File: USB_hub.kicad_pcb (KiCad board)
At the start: 2 copper layers, 127.5 x 50.8 mm, 249 parts, among them J1 USB_SPI_(Opt), J10 USB3_A, J11 Conn_01x02_Socket, J12 USB_C_Receptacle, J13 I2C_HD3SS3220, J2 USB_C_Receptacle, J3 I2C_HD3SS3220, J4 USB_C_Receptacle, J5 I2C2_PD_Controller, J6 I2C_Mux, J7 I2C_EEPROM, J8 SD_Card_Receptacle, J9 USB3_A, Q1 SiRA24DP, Q2 SiRA12DP, SW1 RESET_HUB, SW2 FW_Upgrade, U1 USB7206C/KDX, U10 M24256-BWMN6P, U11 TPD4E02B04DQA, U12 TPD4E02B04DQA, U13 TPD4E02B04DQA, U14 TUSB1142IRNQR_C5216209, U15 GL3224-OIY04, U16 UCS2113-1-V/G4, U17 TPD4E02B04DQA, U18 TPD4E02B04DQA, U19 MCP19035-BAABE/MF, U2 MIC803-29D4VM3-TR, U20 TPS7A4701xRGW, U21 MIC23201YML-TR, U22 HD3SS3220IRNHR, U23 TPD4E02B04DQA, U24 TPD4E02B04DQA, U25 TPD4E02B04DQA, U3 HD3SS3220IRNHR, U4 TPS2068EDBVR, U5 TPD4E02B04DQA, U6 TPD4E02B04DQA, U7 TPD4E02B04DQA, U8 TVS2200DRV, U9 TPS25762CQRQLRQ1, Y1 25MHz, Y2 25MHz +-0.03%

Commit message: footprints grouped by the function
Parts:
- R1, R10, R11, R12, R13, R14, R15, R16, R17, R18, R19, R2, R20, R21, R22, R24, R25, R26, R27, R28, R29, R3, R30, R31, R32, R33, R34, R35, R36, R37, R38, R39, R4, R40, R41, R42, R43, R44, R45, R46, R47, R48, R49, R5, R50, R51, R52, R53, R54, R55, R56, R57, R58, R59, R6, R60, R61, R62, R63, R64, R65, R66, R67, R7, R8, R9: footprint Resistor_SMD:R_0603_1608Metric -> Resistor_SMD:R_0402_1005Metric
- R23: footprint Resistor_SMD:R_0603_1608Metric -> Resistor_SMD:R_1206_3216Metric
- moved C80 194.3 mm to (260.9, 130.6), turned to 90 degrees
- moved C79 183.4 mm to (249.3, 130.6), turned to 90 degrees
- moved C78 173.5 mm to (237.8, 130.6), turned to 90 degrees
- moved C77 164.6 mm to (226.2, 130.6), turned to 90 degrees
- moved C22 130.3 mm to (112.8, 168.1)
- moved U16 124.1 mm to (216.8, 130.9)
- moved NT1 122.2 mm to (-69.3, 22.8)
- moved C50 122.2 mm to (-99.3, 47.9)
- moved TP3 122.2 mm to (-57.5, 56.5)
- moved TP4 122.2 mm to (-57.5, 61.2)
- moved U9 122.2 mm to (-51.5, 36.3), turned to 180 degrees
- moved R2 122.0 mm to (235.3, 165.3), turned to -90 degrees
- moved R47 121.4 mm to (216.7, 135.4), turned to 90 degrees
- moved C81 121.1 mm to (219.9, 129.4), turned to 90 degrees
- moved J1 120.7 mm to (241.3, 162.3), turned to 180 degrees
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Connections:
- C20 pad 2: /USB7206C/XIN -> /USB7206C/XTALI
- C21 pad 2: /USB7206C/XOUT -> /USB7206C/XTALO
- Y1 pad 1: /USB7206C/XIN -> /USB7206C/XTALI
- Y1 pad 4: /USB7206C/XOUT -> /USB7206C/XTALO
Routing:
- net Net-(U1B-TEST1): track 0.00 -> 8.92 mm
- net Net-(U1B-TEST2): track 0.00 -> 7.05 mm
- net Net-(U1B-TEST3): track 0.00 -> 5.30 mm
- net GND: track 2.30 -> 4.57 mm

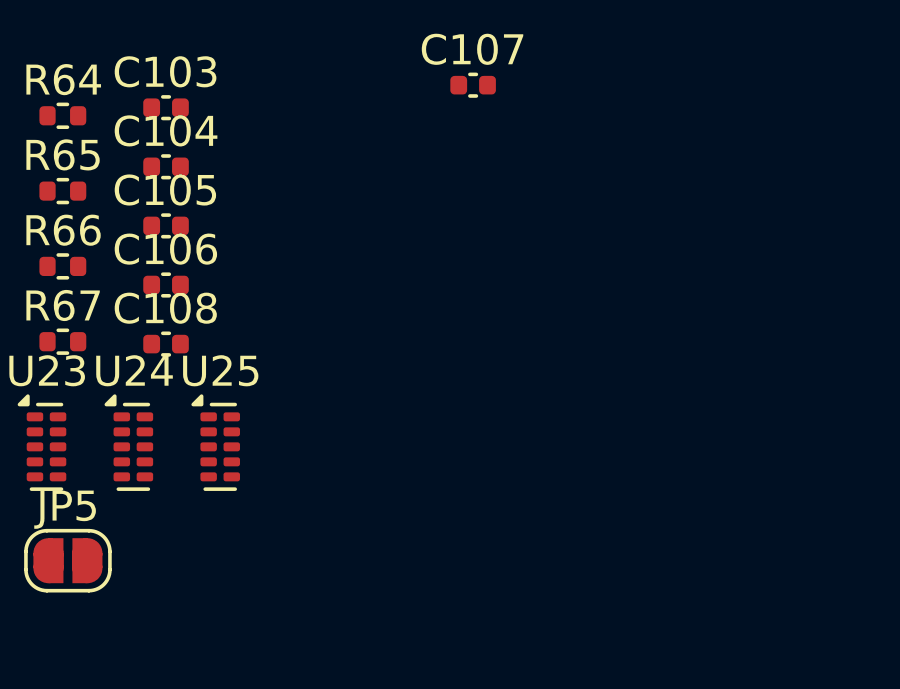
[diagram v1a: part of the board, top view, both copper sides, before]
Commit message: Scheme fixes
Fixed wrong connection of SNS pin of U21
USB7206c symbol improved
R7's value fixed
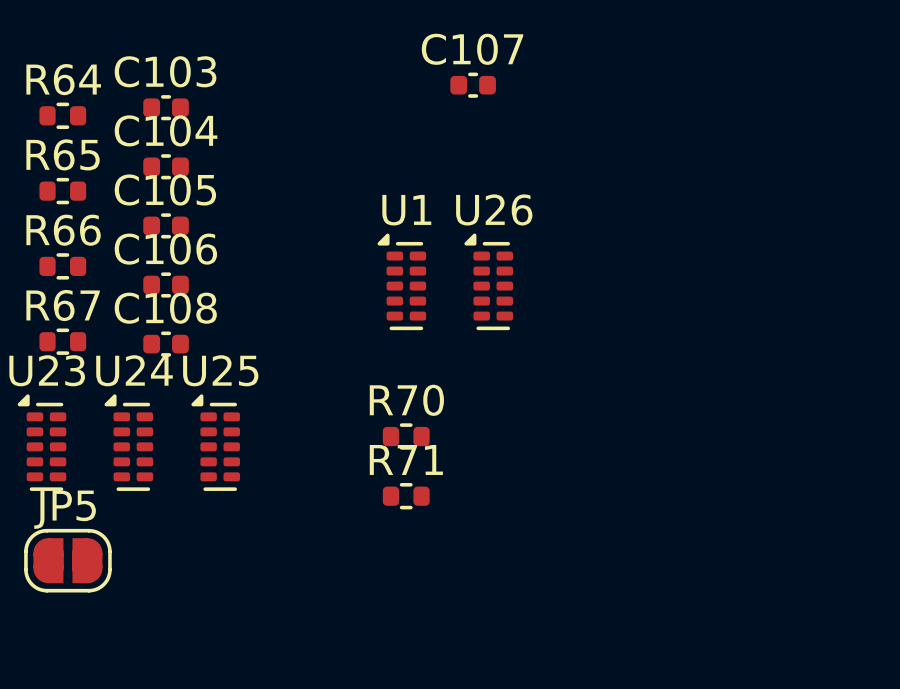
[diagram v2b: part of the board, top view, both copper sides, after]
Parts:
- added R70: 200k, Resistor_SMD:R_0402_1005Metric, F.Cu at (55.9, 132.4)
- added R71: 10k, Resistor_SMD:R_0402_1005Metric, F.Cu at (55.9, 134.4)
- added U1: TPD4E02B04DQA, Package_SON:USON-10_2.5x1.0mm_P0.5mm, F.Cu at (55.9, 127.4)
- added U26: TPD4E02B04DQA, Package_SON:USON-10_2.5x1.0mm_P0.5mm, F.Cu at (58.8, 127.4)
- R6: value 100k -> 200k
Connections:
- net Net-(U4-~{FLT}) renamed /USB-C1/~{FLT}
- J12 pad A6: /USB7206C/USB3UP.D+ -> /USB7206C/USB3_UP.D+
- J12 pad A7: /USB7206C/USB3UP.D- -> /USB7206C/USB3_UP.D-
- J12 pad B6: /USB7206C/USB3UP.D+ -> /USB7206C/USB3_UP.D+
- J12 pad B7: /USB7206C/USB3UP.D- -> /USB7206C/USB3_UP.D-
- R1 pad 1: Net-(U1B-RBIAS) -> Net-(U27-RBIAS)
- R1 pad 2: VSS -> GND
- R11 pad 1: VBUS_C1 -> +5V
- R2 pad 2: Net-(U1B-TEST1) -> Net-(U27-TEST1)
- R3 pad 2: Net-(U1B-TEST2) -> Net-(U27-TEST2)
- R4 pad 2: Net-(U1B-TEST3) -> Net-(U27-TEST3)
- U11 pad 10: unconnected-(U11-NC-Pad10) -> /USB-C2/USB-C2.RX1-
- U11 pad 6: unconnected-(U11-NC-Pad6) -> /USB-C2/USB-C2.TX1+
- U11 pad 7: unconnected-(U11-NC-Pad7) -> /USB-C2/USB-C2.TX1-
- U11 pad 9: unconnected-(U11-NC-Pad9) -> /USB-C2/USB-C2.RX1+
- U12 pad 10: unconnected-(U12-NC-Pad10) -> /USB-C2/USB-C2.RX2-
- U12 pad 6: unconnected-(U12-NC-Pad6) -> /USB-C2/USB-C2.TX2+
- U12 pad 7: unconnected-(U12-NC-Pad7) -> /USB-C2/USB-C2.TX2-
- U12 pad 9: unconnected-(U12-NC-Pad9) -> /USB-C2/USB-C2.RX2+
- U13 pad 10: unconnected-(U13-NC-Pad10) -> /USB-C2/USB-C2.CC1
- U13 pad 6: unconnected-(U13-NC-Pad6) -> /USB-C2/USB3_IN.D+
- U13 pad 7: unconnected-(U13-NC-Pad7) -> /USB-C2/USB3_IN.D-
- U13 pad 9: unconnected-(U13-NC-Pad9) -> /USB-C2/USB-C2.CC2
- U17 pad 10: unconnected-(U17-NC-Pad10) -> /USB-A1/USB-A1.RX1-
- U17 pad 6: unconnected-(U17-NC-Pad6) -> /USB-A1/USB-A1.TX1+
- U17 pad 7: unconnected-(U17-NC-Pad7) -> /USB-A1/USB-A1.TX1-
- U17 pad 9: unconnected-(U17-NC-Pad9) -> /USB-A1/USB-A1.RX1+
- U18 pad 10: unconnected-(U18-NC-Pad10) -> /USB-A1/USB-A2.RX1-
- U18 pad 6: unconnected-(U18-NC-Pad6) -> /USB-A1/USB-A2.TX1+
- U18 pad 7: unconnected-(U18-NC-Pad7) -> /USB-A1/USB-A2.TX1-
- U18 pad 9: unconnected-(U18-NC-Pad9) -> /USB-A1/USB-A2.RX1+
- U22 pad 10: /USB7206C/USB3UP.RX1- -> /USB7206C/USB3_UP.RX1-
- U22 pad 6: /USB7206C/USB3UP.TX1+ -> /USB7206C/USB3_UP.TX1+
- U22 pad 7: /USB7206C/USB3UP.TX1- -> /USB7206C/USB3_UP.TX1-
- U22 pad 9: /USB7206C/USB3UP.RX1+ -> /USB7206C/USB3_UP.RX1+
- U23 pad 10: unconnected-(U23-NC-Pad10) -> /USB-C_UP/USB-C_UP1/USB-C1.CC1
- U23 pad 6: unconnected-(U23-NC-Pad6) -> /USB-C_UP/USB-C_UP1/USB-C1.D+
- U23 pad 7: unconnected-(U23-NC-Pad7) -> /USB-C_UP/USB-C_UP1/USB-C1.D-
- U23 pad 9: unconnected-(U23-NC-Pad9) -> /USB-C_UP/USB-C_UP1/USB-C1.CC2
- U24 pad 10: unconnected-(U24-NC-Pad10) -> /USB-C_UP/USB-C_UP1/USB-C1.RX2-
- U24 pad 6: unconnected-(U24-NC-Pad6) -> /USB-C_UP/USB-C_UP1/USB-C1.TX2+
- U24 pad 7: unconnected-(U24-NC-Pad7) -> /USB-C_UP/USB-C_UP1/USB-C1.TX2-
- U24 pad 9: unconnected-(U24-NC-Pad9) -> /USB-C_UP/USB-C_UP1/USB-C1.RX2+
- U25 pad 10: unconnected-(U25-NC-Pad10) -> /USB-C_UP/USB-C_UP1/USB-C1.RX1-
- U25 pad 6: unconnected-(U25-NC-Pad6) -> /USB-C_UP/USB-C_UP1/USB-C1.TX1+
- U25 pad 7: unconnected-(U25-NC-Pad7) -> /USB-C_UP/USB-C_UP1/USB-C1.TX1-
- U25 pad 9: unconnected-(U25-NC-Pad9) -> /USB-C_UP/USB-C_UP1/USB-C1.RX1+
- U5 pad 10: unconnected-(U5-NC-Pad10) -> /USB-C1/USB-C1.CC1
- U5 pad 6: unconnected-(U5-NC-Pad6) -> /USB-C1/USB-C1.D+
- U5 pad 7: unconnected-(U5-NC-Pad7) -> /USB-C1/USB-C1.D-
- U5 pad 9: unconnected-(U5-NC-Pad9) -> /USB-C1/USB-C1.CC2
- U6 pad 10: unconnected-(U6-NC-Pad10) -> /USB-C1/USB-C1.RX2-
- U6 pad 6: unconnected-(U6-NC-Pad6) -> /USB-C1/USB-C1.TX2+
- U6 pad 7: unconnected-(U6-NC-Pad7) -> /USB-C1/USB-C1.TX2-
- U6 pad 9: unconnected-(U6-NC-Pad9) -> /USB-C1/USB-C1.RX2+
- U7 pad 10: unconnected-(U7-NC-Pad10) -> /USB-C1/USB-C1.RX1-
- U7 pad 6: unconnected-(U7-NC-Pad6) -> /USB-C1/USB-C1.TX1+
- U7 pad 7: unconnected-(U7-NC-Pad7) -> /USB-C1/USB-C1.TX1-
- U7 pad 9: unconnected-(U7-NC-Pad9) -> /USB-C1/USB-C1.RX1+

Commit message: Board set-up setted, Scheme pdf exported,
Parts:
- removed the C101 at (58.6, 109.9)
- removed the C102 at (22.9, 114.7)
- removed the C103 at (47.9, 121.5)
- removed the C82 at (181.7, 13.5)
- removed the C83 at (181.7, 12.4)
- removed the C84 at (176.6, 12.3)
- removed JP3: SMCLK, Jumper:SolderJumper-2_P1.3mm_Open_Pad1.0x1.5mm
- removed JP4: SM_BUS or Standalone, Jumper:SolderJumper-3_P1.3mm_Open_RoundedPad1.0x1.5mm_NumberLabels
- removed JP5: Connect to I2C mode, Jumper:SolderJumper-2_P1.3mm_Open_RoundedPad1.0x1.5mm
- removed Q2: SiRA12DP, Package_SO:PowerPAK_SO-8_Single
- removed the R47 at (216.7, 135.4)
- removed the R50 at (212.1, 123.4)
- removed the R51 at (212.2, 120.8)
- removed the R52 at (184.5, 9.50)
- removed the R53 at (180.1, 12.9)
- removed the R54 at (173.8, 14.1)
- removed the R55 at (173.8, 12.3)
- removed the R56 at (178.6, 11.5)
- removed the R57 at (186.2, 17.0)
- removed the R62 at (55.2, 110.2)
- removed the R63 at (55.2, 112.7)
- removed TP13: Out2, TestPoint:TestPoint_2Pads_Pitch5.08mm_Drill1.3mm
- removed the TP7 at (215.4, 11.0)
- removed the U1 at (55.9, 127.4)
- removed the U1 at (219.2, 165.2)
- removed the U19 at (186.8, 12.8)
- removed the U20 at (171.1, 45.0)
- removed the U25 at (49.7, 132.8)
- added C100: 1uF, Capacitor_SMD:C_0402_1005Metric, F.Cu at (352.6, -21.5)
- added C109: 47uF, Capacitor_SMD:C_0402_1005Metric, F.Cu at (355.4, -23.4)
- added C110: 47uF, Capacitor_SMD:C_0402_1005Metric, F.Cu at (355.4, -21.5)
- added C111: 47uF, Capacitor_SMD:C_0402_1005Metric, F.Cu at (355.4, -19.5)
- added C112: 100nF, Capacitor_SMD:C_0402_1005Metric, F.Cu at (374.6, -24.5)
- added C113: 22nF, Capacitor_SMD:C_0402_1005Metric, F.Cu at (376.3, -25.1)
- added C121: 100uF, Capacitor_THT:C_Radial_D10.0mm_H16.0mm_P5.00mm, F.Cu at (443.8, 38.8)
- added C122: 100nF, Capacitor_SMD:C_0402_1005Metric, F.Cu at (450.9, 21.4)
- added C123: 100nF, Capacitor_SMD:C_0402_1005Metric, F.Cu at (450.9, 23.3)
- added C124: 100nF, Capacitor_SMD:C_0402_1005Metric, F.Cu at (450.9, 25.3)
- added C125: 100nF, Capacitor_SMD:C_0402_1005Metric, F.Cu at (450.9, 27.3)
- added C126: 100nF, Capacitor_SMD:C_0402_1005Metric, F.Cu at (450.9, 29.2)
- added C20: 10uF, Capacitor_SMD:C_0402_1005Metric, F.Cu at (443.7, 55.8)
- added C74: 330nF, Capacitor_SMD:C_0402_1005Metric, F.Cu at (403.3, 61.8)
- added C75: 330nF, Capacitor_SMD:C_0402_1005Metric, F.Cu at (403.3, 63.8)
- added C91: 1u, Capacitor_SMD:C_0402_1005Metric, F.Cu at (478.0, -40.7)
- added C92: 0.1u, Capacitor_SMD:C_0402_1005Metric, F.Cu at (479.3, -40.7)
- added C93: 1u, Capacitor_SMD:C_0402_1005Metric, F.Cu at (478.0, -48.5)
- added C94: 0.1u, Capacitor_SMD:C_0402_1005Metric, F.Cu at (479.3, -48.5)
- added C95: 1uF, Capacitor_SMD:C_0402_1005Metric, F.Cu at (378.6, -22.6)
- added C96: 10uF, Capacitor_SMD:C_0402_1005Metric, F.Cu at (349.7, -15.6)
- added C97: 10uF, Capacitor_SMD:C_0402_1005Metric, F.Cu at (349.7, -13.6)
- added C98: 10uF, Capacitor_SMD:C_0402_1005Metric, F.Cu at (349.7, -11.6)
- added C99: 1uF, Capacitor_SMD:C_0402_1005Metric, F.Cu at (352.6, -23.4)
- added D1: ESD441DPLR, EasyEDA:X2SON-2_L0.6-W0.3-P0.35, F.Cu at (443.2, 57.6)
- added D12: B520C-13-F, Diode_SMD:D_SMC, F.Cu at (573.9, 58.8)
- added D13: SMCJ12A, Diode_SMD:D_SMC, F.Cu at (539.2, 61.3)
- added D14: GREEN, LED_SMD:LED_0603_1608Metric, F.Cu at (486.9, 142.6)
- added D15: GREEN, LED_SMD:LED_0603_1608Metric, F.Cu at (553.2, 85.3)
- added D16: GREEN, LED_SMD:LED_0603_1608Metric, F.Cu at (553.2, 87.4)
- added D17: GREEN, LED_SMD:LED_0603_1608Metric, F.Cu at (553.2, 89.3)
- added D2: ESD441DPLR, EasyEDA:X2SON-2_L0.6-W0.3-P0.35, F.Cu at (396.8, 62.5)
- added D3: LED, LED_SMD:LED_0603_1608Metric, F.Cu at (397.9, 57.8)
- added D4: GREEN, LED_SMD:LED_0603_1608Metric, F.Cu at (397.9, 60.4)
- added FB1: 7427934, SamacSys_Parts:7427934, F.Cu at (470.7, -55.5)
- added FB2: 7427934, SamacSys_Parts:7427934, F.Cu at (470.8, -38.5)
- added FB3: 7427934, SamacSys_Parts:7427934, F.Cu at (470.8, -46.4)
- added R13: 200k, Resistor_SMD:R_0402_1005Metric, F.Cu at (394.4, 57.5)
- added R17: 5k, Resistor_SMD:R_0402_1005Metric, F.Cu at (394.4, 59.5)
- added R18: 4.7k, Resistor_SMD:R_0402_1005Metric, F.Cu at (394.4, 61.5)
- added R19: 1.5k, Resistor_SMD:R_0402_1005Metric, F.Cu at (394.4, 63.5)
- added R20: 4.7k, Resistor_SMD:R_0402_1005Metric, F.Cu at (394.4, 65.5)
- added R35: 4.7k, Resistor_SMD:R_0402_1005Metric, F.Cu at (448.6, 51.8)
- added R36: 4.7k, Resistor_SMD:R_0402_1005Metric, F.Cu at (448.6, 53.8)
- added R37: 4.7k, Resistor_SMD:R_0402_1005Metric, F.Cu at (448.6, 55.8)
- added R38: 4.7k, Resistor_SMD:R_0402_1005Metric, F.Cu at (448.6, 57.8)
- added R43: 1k, Resistor_SMD:R_0402_1005Metric, F.Cu at (448.6, 59.8)
- added R5: 33k, Resistor_SMD:R_0402_1005Metric, F.Cu at (443.7, 51.8)
- added R59: 520, Resistor_SMD:R_0402_1005Metric, F.Cu at (406.2, 61.8)
- added R6: 50k, Resistor_SMD:R_0402_1005Metric, F.Cu at (443.7, 53.8)
- added R68: 2, Resistor_SMD:R_0402_1005Metric, F.Cu at (478.0, -59.3)
- added R69: 200, Resistor_SMD:R_0402_1005Metric, F.Cu at (558.4, 58.0)
- added R70: 27k, Resistor_SMD:R_0402_1005Metric, F.Cu at (548.1, 60.3)
- added R71: 47k, Resistor_SMD:R_0402_1005Metric, F.Cu at (548.1, 61.5)
- added R72: 100 1%, Resistor_SMD:R_0402_1005Metric, F.Cu at (552.3, 63.4)
- added R73: 549 1%, Resistor_SMD:R_0402_1005Metric, F.Cu at (553.5, 63.4)
- added R74: 2, Resistor_SMD:R_0402_1005Metric, F.Cu at (478.7, -42.3)
- added R75: 2, Resistor_SMD:R_0402_1005Metric, F.Cu at (478.7, -50.2)
- added R76: 290k, Resistor_SMD:R_0402_1005Metric, F.Cu at (378.0, -20.7)
- added R77: 10k, Resistor_SMD:R_0402_1005Metric, F.Cu at (370.8, -21.2)
- added R78: 5k, Resistor_SMD:R_0402_1005Metric, F.Cu at (372.2, -25.3)
- added R79: 680, Resistor_SMD:R_0402_1005Metric, F.Cu at (372.9, -23.5)
- added R80: 243k, Resistor_SMD:R_0402_1005Metric, F.Cu at (376.3, -24.0)
- added R81: R, Resistor_SMD:R_0402_1005Metric, F.Cu at (376.3, -22.9)
- added R82: 560, Resistor_SMD:R_0402_1005Metric, F.Cu at (486.7, 140.8)
- added R83: 10k, Resistor_SMD:R_0402_1005Metric, F.Cu at (487.6, 144.4)
- added R84: 4.7k, Resistor_SMD:R_0402_1005Metric, F.Cu at (550.3, 85.3)
- added R85: 1.5k, Resistor_SMD:R_0402_1005Metric, F.Cu at (550.3, 87.4)
- added R86: 560, Resistor_SMD:R_0402_1005Metric, F.Cu at (550.3, 89.3)
- added R87: 1M, Resistor_SMD:R_0402_1005Metric, F.Cu at (491.5, 146.2)
- added R92: 900k, Resistor_SMD:R_0402_1005Metric, F.Cu at (439.1, 34.0)
- added R93: 200k, Resistor_SMD:R_0402_1005Metric, F.Cu at (439.1, 36.0)
- added R94: 200k, Resistor_SMD:R_0402_1005Metric, F.Cu at (439.1, 38.0)
- added R95: 4.7k, Resistor_SMD:R_0402_1005Metric, F.Cu at (439.1, 40.0)
- added R96: 4.7k, Resistor_SMD:R_0402_1005Metric, F.Cu at (439.1, 42.0)
- added R97: 4.7k, Resistor_SMD:R_0402_1005Metric, F.Cu at (439.1, 44.0)
- added TP9: 0 when there is a connected device & port is fuctioning as 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, TestPoint:TestPoint_Loop_D1.80mm_Drill1.0mm_Beaded, F.Cu at (430.2, 22.7)
- added U1: USB7206C/KDX, SamacSys_Parts:QFN40P1200X1200X90-101N-D, F.Cu at (219.1, 165.3)
- added U16: TPD4E02B04DQA, Package_SON:USON-10_2.5x1.0mm_P0.5mm, F.Cu at (403.3, 58.8)
- added U17: TPD4E02B04DQA, Package_SON:USON-10_2.5x1.0mm_P0.5mm, F.Cu at (406.2, 58.8)
- added U21: SiRA80DP, Package_SO:PowerPAK_SO-8L_Single, F.Cu at (563.2, 53.1)
- added U27: TPD4E02B04DQA, Package_SON:USON-10_2.5x1.0mm_P0.5mm, F.Cu at (442.0, 46.8)
- added U28: TPD4E02B04DQA, Package_SON:USON-10_2.5x1.0mm_P0.5mm, F.Cu at (444.9, 46.8)
- added U29: TPD4E02B04DQA, Package_SON:USON-10_2.5x1.0mm_P0.5mm, F.Cu at (447.8, 46.8)
- C102: renamed from C91; value 47uF -> 4.7uF
- C104: value 100nF -> 820pF
- C105: value 100nF -> C
- C106, C107, C108: value 100nF -> 47uF
- C42: renamed from C41; value 0.1uF (10V) -> 0.1uF (50V)
- C44: renamed from C43; value 0.1uF (10V) -> 0.1uF (50V)
- C85: value 0.33uF -> 1u
- C86: value 100uF -> 0.1u; footprint Capacitor_THT:C_Radial_D10.0mm_H16.0mm_P5.00mm -> Capacitor_SMD:C_0402_1005Metric
- C87, C88: value 100uF -> 2.2nF; footprint Capacitor_THT:C_Radial_D10.0mm_H16.0mm_P5.00mm -> Capacitor_SMD:C_0402_1005Metric
- C89: value 0.1uF -> 8.20nF
- C90: value 4.7uF -> 4.3nF
- D5: renamed from D1; value LED -> GREEN
- D6: value SMBJP6KE6.8 -> GREEN; footprint Diode_SMD:D_SMB -> LED_SMD:LED_0603_1608Metric
- D7: value ESD441DPLR -> GREEN; footprint EasyEDA:X2SON-2_L0.6-W0.3-P0.35 -> LED_SMD:LED_0603_1608Metric
- J1: footprint Connector_PinHeader_1.27mm:PinHeader_1x05_P1.27mm_Vertical -> Connector_PinHeader_1.27mm:PinHeader_1x06_P1.27mm_Vertical
- J10, J9: footprint Connector_USB:USB3_A_Molex_48393-001 -> SamacSys_Parts:GSB4116344HR
- J11: value Conn_01x02_Socket -> 8-pin ATX connector; footprint Connector_PinHeader_1.27mm:PinHeader_1x02_P1.27mm_Vertical -> SamacSys_Parts:45586-000Y
- J2, J4: footprint Connector_USB:USB_C_Receptacle_Amphenol_12401610E4-2A -> SamacSys_Parts:USB420003A
- JP2: value SMDATA -> Connect to I2C mode; footprint Jumper:SolderJumper-2_P1.3mm_Open_Pad1.0x1.5mm -> Jumper:SolderJumper-2_P1.3mm_Open_RoundedPad1.0x1.5mm
- L2: value 2uH -> 4.7nH
- Q1: value SiRA24DP -> MMBT2222A; footprint Package_SO:PowerPAK_SO-8_Single -> Package_TO_SOT_SMD:SOT-23-3
- R11: renamed from R7; value 900 -> 900k
- R34: renamed from R25; value R -> 1k
- R64: value 900k -> 1.5k
- R65: value 200k -> 1.5k
- R66: value 200k -> 10k
- R67: value 4.7k -> 499k
- TP1, TP2: footprint TestPoint:TestPoint_2Pads_Pitch5.08mm_Drill1.3mm -> TestPoint:TestPoint_Loop_D1.80mm_Drill1.0mm_Beaded
- TP10: value 0 when there is a connected device & port is fuctioning as DFP -> 0 when overvurrent on VCONN detected; footprint TestPoint:TestPoint_2Pads_Pitch5.08mm_Drill1.3mm -> TestPoint:TestPoint_Loop_D1.80mm_Drill1.0mm_Beaded
- TP11: value 0 when overvurrent on VCONN detected -> Out1; footprint TestPoint:TestPoint_2Pads_Pitch5.08mm_Drill1.3mm -> TestPoint:TestPoint_Loop_D1.80mm_Drill1.0mm_Beaded
- TP12: value Out1 -> Out2; footprint TestPoint:TestPoint_2Pads_Pitch5.08mm_Drill1.3mm -> TestPoint:TestPoint_Loop_D1.80mm_Drill1.0mm_Beaded
- TP3, TP4, TP5, TP6: footprint TestPoint:TestPoint_THTPad_1.5x1.5mm_Drill0.7mm -> TestPoint:TestPoint_Loop_D1.80mm_Drill1.0mm_Beaded
- TP7: renamed from TP8; footprint TestPoint:TestPoint_THTPad_1.5x1.5mm_Drill0.7mm -> TestPoint:TestPoint_Loop_D1.80mm_Drill1.0mm_Beaded
- TP8: renamed from TP9; footprint TestPoint:TestPoint_THTPad_1.5x1.5mm_Drill0.7mm -> TestPoint:TestPoint_Loop_D1.80mm_Drill1.0mm_Beaded
- U10: value M24256-BWMN6P -> 24LC256
- U18: renamed from U16; value UCS2113-1-V/G4 -> UCS2114-1-V/G4
- U22: value HD3SS3220IRNHR -> TPS25983; footprint footprints:RNH0030A -> SamacSys_Parts:TPS259830ONRGER
- U23: value TPD4E02B04DQA -> AP7361C-33E; footprint Package_SON:USON-10_2.5x1.0mm_P0.5mm -> Package_TO_SOT_SMD:SOT-223-3_TabPin2
- U24: value TPD4E02B04DQA -> MP8795; footprint Package_SON:USON-10_2.5x1.0mm_P0.5mm -> Package_DFN_QFN:MPS-QFN-21_3x4mm
- U26: value TPD4E02B04DQA -> HD3SS3220IRNHR; footprint Package_SON:USON-10_2.5x1.0mm_P0.5mm -> footprints:RNH0030A
- moved U22 526.1 mm to (553.2, 58.5)
- moved R66 518.2 mm to (558.4, 60.3), turned to 180 degrees
- moved R67 508.5 mm to (548.1, 59.1)
- moved R65 506.8 mm to (550.2, 91.4)
- moved R64 506.5 mm to (550.2, 93.3)
- moved D7 495.5 mm to (553.2, 91.4), turned to 180 degrees
- moved J12 419.1 mm to (443.6, 26.8)
- moved TP10 418.0 mm to (430.2, 27.3)
- moved TP11 418.0 mm to (430.2, 32.0)
- moved TP12 418.0 mm to (430.2, 36.6)
- moved J13 408.3 mm to (434.4, 40.6)
- moved U26 380.9 mm to (430.1, 42.2)
- moved C90 366.6 mm to (551.2, 63.4), turned to -90 degrees
- moved U24 361.6 mm to (374.7, -19.8), turned to -90 degrees
- moved C104 357.9 mm to (373.5, -25.3), turned to 90 degrees
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- renumbered C93 to C101, C92 to C103, C94 to C114, C95 to C115, C96 to C116, C97 to C117, C98 to C118, C99 to C119, C100 to C120, C20 to C21, C21 to C22, C22 to C23, C23 to C24, C24 to C25, C25 to C26, C26 to C27, C27 to C28, C28 to C29, C29 to C30, C30 to C31, C31 to C32, C32 to C33, C33 to C34, C34 to C35, C35 to C36, C36 to C37, C37 to C38, C38 to C39, C39 to C40, C40 to C41, C42 to C43, C44 to C45, C45 to C46, C46 to C47, C47 to C48, C48 to C49, C49 to C50, C50 to C51, C51 to C52, C52 to C53, C53 to C54, C54 to C55, C55 to C56, C56 to C57, C57 to C58, C58 to C59, C59 to C60, C60 to C61, C61 to C62, C62 to C63, C63 to C64, C64 to C65, C65 to C66, C66 to C67, C67 to C68, C68 to C69, C69 to C70, C70 to C71, C71 to C72, C72 to C73, C73 to C76, C74 to C77, C75 to C78, C76 to C79, C77 to C80, C78 to C81, C79 to C82, C80 to C83, C81 to C84, D4 to D10, D5 to D11, D2 to D8, D3 to D9, R6 to R10, R8 to R12, R9 to R14, R10 to R15, R11 to R16, R12 to R21, R13 to R22, R14 to R23, R15 to R24, R16 to R25, R17 to R26, R18 to R27, R19 to R28, R20 to R29, R21 to R30, R22 to R31, R23 to R32, R24 to R33, R26 to R39, R27 to R40, R28 to R41, R29 to R42, R30 to R44, R31 to R45, R32 to R46, R33 to R47, R34 to R48, R35 to R49, R36 to R50, R37 to R51, R38 to R52, R39 to R53, R40 to R54, R41 to R55, R42 to R56, R43 to R57, R44 to R58, R45 to R60, R46 to R61, R48 to R62, R49 to R63, R71 to R7, R5 to R8, R58 to R88, R59 to R89, R70 to R9, R60 to R90, R61 to R91, U17 to U19, U18 to U20, U21 to U25
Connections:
- net /USB7206C/USB3_UP.D+ renamed /USB-C_UP1/USB3_IN.D+
- net /USB7206C/USB3_UP.D- renamed /USB-C_UP1/USB3_IN.D-
- C101 pad 1: Net-(U20-NR) -> +5V_Power
- C104 pad 1: Net-(U22-TX1P) -> Net-(U24-FB)
- C104 pad 2: /USB-C_UP/USB-C_UP1/USB-C1.TX1+ -> +5V_prefiltered
- C105 pad 1: Net-(U22-TX1N) -> Net-(U24-VCC)
- C105 pad 2: /USB-C_UP/USB-C_UP1/USB-C1.TX1- -> GND
- C106 pad 1: Net-(U22-TX2P) -> +5V_prefiltered
- C106 pad 2: /USB-C_UP/USB-C_UP1/USB-C1.TX2+ -> GND
- C107 pad 1: Net-(U22-TX2N) -> +5V_prefiltered
- C107 pad 2: /USB-C_UP/USB-C_UP1/USB-C1.TX2- -> GND
- C108 pad 1: Net-(U22-TX2N) -> +5V_prefiltered
- C108 pad 2: /USB-C_UP/USB-C_UP1/USB-C1.TX2- -> GND
- C114 pad 1: +5V -> +5V_Power
- C115 pad 1: +5V -> +5V_Power
- C116 pad 1: +5V -> +5V_Power
- C119 pad 1: +5V -> +5V_Power
- C23 pad 1: +5V -> +5V_USB_C_SD
- C24 pad 1: +5V -> +5V_USB_C_SD
- C29 pad 1: +5V -> +5V_USB_C_SD
- C30 pad 1: +5V -> +5V_USB_C_SD
- C80 pad 1: +5V -> +5V_USB_A
- C81 pad 1: +5V -> +5V_USB_A
- C82 pad 1: +5V -> +5V_USB_A
- C83 pad 1: +5V -> +5V_USB_A
- C84 pad 1: +5V -> +5V_USB_A
- C85 pad 1: Net-(U19-BOOT) -> +5V_USB_A
- C85 pad 2: /Power/PHASE -> Net-(C85-Pad2)
- C86 pad 1: +5V -> +5V_USB_A
- C87 pad 1: +5V -> Net-(U22-NRETRY)
- C88 pad 1: +5V -> Net-(U22-RETRY_DLY)
- C89 pad 1: +5V -> Net-(U22-dVdt)
- C90 pad 1: GND -> Net-(U22-ITIMER)
- C90 pad 2: Net-(U19-+VCC) -> GND
- D5 pad 2: /SD-interface/LED -> Net-(D5-A)
- D6 pad 2: +5V -> Net-(D6-A)
- D7 pad 1: VBUS_UP -> GND
- D7 pad 2: GND -> Net-(D7-A)
- J11 pad 1: GND -> Net-(D13-C)
- J11 pad 2: +12V -> Net-(D13-C)
- J12 pad A10: /USB-C_UP/USB-C_UP1/USB-C1.RX2- -> /USB-C_UP1/USB-C1.RX2-
- J12 pad A11: /USB-C_UP/USB-C_UP1/USB-C1.RX2+ -> /USB-C_UP1/USB-C1.RX2+
- J12 pad A2: /USB-C_UP/USB-C_UP1/USB-C1.TX1+ -> /USB-C_UP1/USB-C1.TX1+
- J12 pad A3: /USB-C_UP/USB-C_UP1/USB-C1.TX1- -> /USB-C_UP1/USB-C1.TX1-
- J12 pad A5: /USB-C_UP/USB-C_UP1/USB-C1.CC1 -> /USB-C_UP1/USB-C1.CC1
- J12 pad B10: /USB-C_UP/USB-C_UP1/USB-C1.RX1- -> /USB-C_UP1/USB-C1.RX1-
- J12 pad B11: /USB-C_UP/USB-C_UP1/USB-C1.RX1+ -> /USB-C_UP1/USB-C1.RX1+
- J12 pad B2: /USB-C_UP/USB-C_UP1/USB-C1.TX2+ -> /USB-C_UP1/USB-C1.TX2+
- J12 pad B3: /USB-C_UP/USB-C_UP1/USB-C1.TX2- -> /USB-C_UP1/USB-C1.TX2-
- J12 pad B5: /USB-C_UP/USB-C_UP1/USB-C1.CC2 -> /USB-C_UP1/USB-C1.CC2
- J13 pad 1: /USB-C_UP/USB-C_UP1/I2C_HD3SS3220.SDA -> /USB-C_UP1/I2C_HD3SS3220.SDA
- J13 pad 2: /USB-C_UP/USB-C_UP1/I2C_HD3SS3220.SCL -> /USB-C_UP1/I2C_HD3SS3220.SCL
- J13 pad 3: /USB-C_UP/USB-C_UP1/I2C_HD3SS3220.INT_N -> /USB-C_UP1/I2C_HD3SS3220.INT_N
- JP2 pad 1: Net-(JP2-A) -> +5V_USB_C_SD
- JP2 pad 2: /USB-A1/SMBUS.SDA -> /USB-C_UP1/ADDR
- L2 pad 1: /Power/PHASE -> Net-(U24-SW)
- L2 pad 2: +5V -> +5V_prefiltered
- L3 pad 1: Net-(U21-SNS) -> Net-(U25-SW)
- Q1 pad 1: /Power/PHASE -> Net-(D14-K)
- Q1 pad 2: /Power/PHASE -> Net-(Q1-B)
- Q1 pad 3: /Power/PHASE -> GND
- R14 pad 1: +5V -> +5V_USB_C_SD
- R15 pad 1: +5V -> +5V_USB_C_SD
- R16 pad 1: +5V -> +5V_USB_C_SD
- R60 pad 2: /USB-A1/PRT_CTR1 -> /USB-A1/PRT_EN1
- R63 pad 1: /USB-A1/PRT_CTR2 -> /USB-A1/PRT_EN2
- R64 pad 1: Net-(U22-VBUS_DET) -> VBUS-A1
- R64 pad 2: VBUS_C1 -> Net-(D6-A)
- R65 pad 1: Net-(U22-DIR) -> VBUS-A2
- R65 pad 2: +3V3 -> Net-(D7-A)
- R66 pad 1: /USB-C_UP/USB-C_UP1/I2C_HD3SS3220.INT_N -> +3V3
- R66 pad 2: +3V3 -> Net-(U22-PG)
- R67 pad 1: GND -> Net-(D13-C)
- R67 pad 2: Net-(U22-PORT) -> Net-(U22-EN/UVLO)
- R88 pad 1: +5V -> +5V_Power
- TP10 pad 1: /USB-C_UP/USB-C_UP1/ID -> /USB-C_UP1/VCONN_FAULT_N
- TP11 pad 1: /USB-C_UP/USB-C_UP1/VCONN_FAULT_N -> /USB-C_UP1/I2C_HD3SS3220.SDA
- TP12 pad 1: /USB-C_UP/USB-C_UP1/I2C_HD3SS3220.SDA -> /USB-C_UP1/I2C_HD3SS3220.SCL
- U14 pad 4: unconnected-(U14-~{SLP_S0}-Pad4) -> Net-(U14-~{SLP_S0})
- U15 pad 1: /SD-interface/USB-SD.TX1- -> Net-(U15-TXN)
- U15 pad 2: /SD-interface/USB-SD.TX1+ -> Net-(U15-TXP)
- U18 pad 10: +5V -> +5V_USB_A
- U18 pad 13: /USB-A1/COMM_ILIM -> +5V_USB_A
- U18 pad 17: Net-(JP3-A) -> GND
- U18 pad 18: Net-(JP2-A) -> GND
- U18 pad 3: Net-(U16-~{BOOST}) -> GND
- U18 pad 6: +5V -> +5V_USB_A
- U18 pad 7: +5V -> +5V_USB_A
- U18 pad 8: +5V -> +5V_USB_A
- U18 pad 9: +5V -> +5V_USB_A
- U22 pad 1: /USB-C_UP/USB-C_UP1/USB-C1.CC2 -> Net-(D13-C)
- U22 pad 10: /USB7206C/USB3_UP.RX1- -> Net-(U22-RETRY_DLY)
- U22 pad 11: Net-(U22-DIR) -> Net-(U22-NRETRY)
- U22 pad 12: GND -> Net-(U22-OVLO)
- U22 pad 13: GND -> Net-(U22-PG)
- U22 pad 14: /USB-C_UP/USB-C_UP1/USB-C1.RX1- -> GND
- U22 pad 15: /USB-C_UP/USB-C_UP1/USB-C1.RX1+ -> Net-(U22-dVdt)
- U22 pad 16: Net-(U22-TX1N) -> (no net)
- U22 pad 17: Net-(U22-TX1P) -> Net-(U21-S-Pad1)
- U22 pad 18: /USB-C_UP/USB-C_UP1/USB-C1.RX2- -> Net-(U21-S-Pad1)
- U22 pad 19: /USB-C_UP/USB-C_UP1/USB-C1.RX2+ -> Net-(U21-S-Pad1)
- U22 pad 2: /USB-C_UP/USB-C_UP1/USB-C1.CC1 -> Net-(D13-C)
- U22 pad 20: Net-(U22-TX2N) -> Net-(U21-S-Pad1)
- U22 pad 21: Net-(U22-TX2P) -> Net-(U21-S-Pad1)
- U22 pad 22: /USB-C_UP/USB-C_UP1/ADDR -> Net-(U21-S-Pad1)
- U22 pad 23: /USB-C_UP/USB-C_UP1/I2C_HD3SS3220.INT_N -> Net-(U21-S-Pad1)
- U22 pad 24: /USB-C_UP/USB-C_UP1/VCONN_FAULT_N -> Net-(U21-S-Pad1)
- U22 pad 25: /USB-C_UP/USB-C_UP1/I2C_HD3SS3220.SDA -> Net-(U21-S-Pad1)
- U22 pad 26: /USB-C_UP/USB-C_UP1/I2C_HD3SS3220.SCL -> GND
- U22 pad 3: unconnected-(U22-CURRENT_MODE-Pad3) -> Net-(D13-C)
- U22 pad 4: Net-(U22-PORT) -> GND
- U22 pad 5: Net-(U22-VBUS_DET) -> GND
- U22 pad 6: /USB7206C/USB3_UP.TX1+ -> Net-(U22-EN/UVLO)
- U22 pad 7: /USB7206C/USB3_UP.TX1- -> Net-(U22-ITIMER)
- U22 pad 8: +3V3 -> Net-(U22-ILIM)
- U22 pad 9: /USB7206C/USB3_UP.RX1+ -> Net-(U22-IMON)
- U23 pad 1: /USB-C_UP/USB-C_UP1/USB-C1.CC1 -> +5V_Power
- U23 pad 2: /USB-C_UP/USB-C_UP1/USB-C1.CC2 -> GND
- U23 pad 3: GND -> +3V3
- U24 pad 1: /USB-C_UP/USB-C_UP1/USB-C1.RX2- -> Net-(U24-BST)
- U24 pad 10: /USB-C_UP/USB-C_UP1/USB-C1.RX2- -> +12V
- U24 pad 2: /USB-C_UP/USB-C_UP1/USB-C1.RX2+ -> AGND
- U24 pad 3: GND -> Net-(U24-CS)
- U24 pad 4: /USB-C_UP/USB-C_UP1/USB-C1.TX2- -> Net-(U24-MODE)
- U24 pad 5: /USB-C_UP/USB-C_UP1/USB-C1.TX2+ -> Net-(U24-SS)
- U24 pad 6: /USB-C_UP/USB-C_UP1/USB-C1.TX2+ -> GND
- U24 pad 7: /USB-C_UP/USB-C_UP1/USB-C1.TX2- -> Net-(U24-FB)
- U24 pad 8: GND -> Net-(U24-EN)
- U24 pad 9: /USB-C_UP/USB-C_UP1/USB-C1.RX2+ -> Net-(U24-PGOOD)
- U25 pad 1: Net-(U21-SNS) -> Net-(U25-SW)
- U25 pad 3: Net-(U21-SNS) -> VCORE
- U25 pad 8: +5V -> +5V_Power
- U25 pad 9: +5V -> +5V_Power
- U26 pad 1: /USB-C_UP/USB-E/USB3_UP.RX1- -> /USB-C_UP1/USB-C1.CC2
- U26 pad 10: /USB-C_UP/USB-E/USB3_UP.RX1- -> /USB-C_UP1/USB3_IN.RX1-
- U26 pad 2: /USB-C_UP/USB-E/USB3_UP.RX1+ -> /USB-C_UP1/USB-C1.CC1
- U26 pad 3: GND -> unconnected-(U26-CURRENT_MODE-Pad3)
- U26 pad 4: /USB-C_UP/USB-E/USB3_UP.TX1- -> Net-(U26-PORT)
- U26 pad 5: /USB-C_UP/USB-E/USB3_UP.TX1+ -> Net-(U26-VBUS_DET)
- U26 pad 6: /USB-C_UP/USB-E/USB3_UP.TX1+ -> /USB-C_UP1/USB3_IN.TX1+
- U26 pad 7: /USB-C_UP/USB-E/USB3_UP.TX1- -> /USB-C_UP1/USB3_IN.TX1-
- U26 pad 8: GND -> +3V3
- U26 pad 9: /USB-C_UP/USB-E/USB3_UP.RX1+ -> /USB-C_UP1/USB3_IN.RX1+
- U3 pad 30: +5V -> +5V_USB_C_SD
- U4 pad 5: +5V -> +5V_USB_C_SD
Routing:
- net Net-(U1B-TEST1): track 8.92 -> 0.00 mm
- net Net-(U1-TEST1): track 0.00 -> 8.92 mm
- net Net-(U1B-TEST2): track 7.05 -> 0.00 mm
- net Net-(U1-TEST2): track 0.00 -> 7.05 mm
- net Net-(U25-SW): track 0.00 -> 5.31 mm
- net Net-(U1B-TEST3): track 5.30 -> 0.00 mm
- net Net-(U1-TEST3): track 0.00 -> 5.30 mm
- net VCORE: track 0.00 -> 5.21 mm
- net Net-(U22-dVdt): track 0.00 -> 4.58 mm
- net Net-(U22-EN/UVLO): track 0.00 -> 4.54 mm
- net GND: track 4.57 -> 8.79 mm
- net Net-(U21-G): track 0.00 -> 4.09 mm
- net Net-(U25-EN): track 5.61 -> 1.91 mm, vias 2 -> 0
- net Net-(U22-NRETRY): track 0.00 -> 3.27 mm
- net Net-(U22-PG): track 0.00 -> 3.07 mm
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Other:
- copper layers 2 -> 6

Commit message: scheme regenerated
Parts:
- removed D11, D9: ESD122DMXR, EasyEDA:X2SON-3_L1.0-W0.6-L
- added U32: TPD4E02B04DQA, Package_SON:USON-10_2.5x1.0mm_P0.5mm, F.Cu at (231.5, -136.9)
- C105: value C -> 1u
- C56, U10, U27: moved to B.Cu
- R81: value R -> 8.2k
- moved TH1 439.3 mm to (318.4, -184.2), turned to -90 degrees
- moved NT1 437.7 mm to (325.8, -165.7)
- moved R34 436.7 mm to (318.5, -181.6), turned to 90 degrees
- moved C36 434.9 mm to (323.9, -170.4), turned to 90 degrees
- moved C32 433.7 mm to (320.6, -175.1), turned to 0 degrees
- moved C33 432.7 mm to (320.6, -174.0), turned to 0 degrees
- moved C54 431.6 mm to (322.8, -168.9), turned to -90 degrees
- moved C39 431.3 mm to (318.5, -176.3), turned to 0 degrees
- moved C37 431.1 mm to (321.7, -170.4), turned to 90 degrees
- moved C40 430.2 mm to (318.5, -175.2), turned to 0 degrees
- moved C55 429.0 mm to (321.7, -168.2), turned to -90 degrees
- moved C48 426.5 mm to (316.3, -175.3), turned to 0 degrees
- moved R32 426.3 mm to (314.4, -178.0), turned to 180 degrees
- moved C49 425.3 mm to (316.3, -174.1), turned to 0 degrees
- moved R31 423.3 mm to (314.4, -175.5), turned to 90 degrees
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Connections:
- net Net-(U14-CRX1n) renamed /USB-C2/CRX1+
- net Net-(U14-CRX1p) renamed /USB-C2/CRX1-
- net Net-(U14-CRX2n) renamed /USB-C2/CRX2-
- net Net-(U14-CRX2p) renamed /USB-C2/CRX2+
- net Net-(U14-CTX1n) renamed /USB-C2/CTX1+
- net Net-(U14-CTX1p) renamed /USB-C2/CTX1-
- net Net-(U14-CTX2n) renamed /USB-C2/CTX2-
- net Net-(U14-CTX2p) renamed /USB-C2/CTX2+
- C50 pad 1: Net-(U9-OUT) -> Net-(C50-Pad1)
- R31 pad 2: Net-(U9-OUT) -> Net-(C50-Pad1)
- R32 pad 1: Net-(U9-OUT) -> VBUS
- R32 pad 2: VBUS -> Net-(C50-Pad1)
- U1 pad 14: /USB-C2/USB3_IN.D+ -> /USB-A1/USB-A2.D+
- U1 pad 15: /USB-C2/USB3_IN.D- -> /USB-A1/USB-A2.D-
- U1 pad 16: /USB-C2/USB3_IN.TX1+ -> /USB-A1/USB-A2.TX1+
- U1 pad 17: /USB-C2/USB3_IN.TX1- -> /USB-A1/USB-A2.TX1-
- U1 pad 19: /USB-C2/USB3_IN.RX1+ -> /USB-A1/USB-A2.RX1+
- U1 pad 20: /USB-C2/USB3_IN.RX1- -> /USB-A1/USB-A2.RX1-
- U1 pad 27: /USB-A1/USB-A2.D+ -> /USB-A1/USB-A1.D+
- U1 pad 28: /USB-A1/USB-A2.D- -> /USB-A1/USB-A1.D-
- U1 pad 29: /USB-A1/USB-A2.TX1+ -> /USB-A1/USB-A1.TX1+
- U1 pad 30: /USB-A1/USB-A2.TX1- -> /USB-A1/USB-A1.TX1-
- U1 pad 32: /USB-A1/USB-A2.RX1+ -> /USB-A1/USB-A1.RX1+
- U1 pad 33: /USB-A1/USB-A2.RX1- -> /USB-A1/USB-A1.RX1-
- U1 pad 34: /USB-A1/USB-A1.D+ -> /SD-interface/USB-SD.D+
- U1 pad 35: /USB-A1/USB-A1.D- -> /SD-interface/USB-SD.D-
- U1 pad 36: /USB-A1/USB-A1.TX1+ -> /SD-interface/USB-SD.TX1+
- U1 pad 37: /USB-A1/USB-A1.TX1- -> /SD-interface/USB-SD.TX1-
- U1 pad 39: /USB-A1/USB-A1.RX1+ -> /SD-interface/USB-SD.RX1+
- U1 pad 40: /USB-A1/USB-A1.RX1- -> /SD-interface/USB-SD.RX1-
- U1 pad 81: /SD-interface/USB-SD.D+ -> /USB-C2/USB3_IN.D+
- U1 pad 82: /SD-interface/USB-SD.D- -> /USB-C2/USB3_IN.D-
- U1 pad 83: /SD-interface/USB-SD.TX1+ -> /USB-C2/USB3_IN.TX1+
- U1 pad 84: /SD-interface/USB-SD.TX1- -> /USB-C2/USB3_IN.TX1-
- U1 pad 86: /SD-interface/USB-SD.RX1+ -> /USB-C2/USB3_IN.RX1+
- U1 pad 87: /SD-interface/USB-SD.RX1- -> /USB-C2/USB3_IN.RX1-
- U11 pad 1: /USB-C2/USB-C2.RX1- -> /USB-C2/USB-C2.RX1+
- U11 pad 10: /USB-C2/USB-C2.RX1- -> /USB-C2/USB-C2.RX1+
- U11 pad 2: /USB-C2/USB-C2.RX1+ -> /USB-C2/USB-C2.RX1-
- U11 pad 4: /USB-C2/USB-C2.TX1- -> /USB-C2/USB-C2.TX2-
- U11 pad 5: /USB-C2/USB-C2.TX1+ -> /USB-C2/USB-C2.TX2+
- U11 pad 6: /USB-C2/USB-C2.TX1+ -> /USB-C2/USB-C2.TX2+
- U11 pad 7: /USB-C2/USB-C2.TX1- -> /USB-C2/USB-C2.TX2-
- U11 pad 9: /USB-C2/USB-C2.RX1+ -> /USB-C2/USB-C2.RX1-
- U12 pad 1: /USB-C2/USB-C2.RX2- -> /USB-C2/USB-C2.RX2+
- U12 pad 10: /USB-C2/USB-C2.RX2- -> /USB-C2/USB-C2.RX2+
- U12 pad 2: /USB-C2/USB-C2.RX2+ -> /USB-C2/USB-C2.RX2-
- U12 pad 4: /USB-C2/USB-C2.TX2- -> /USB-C2/USB-C2.TX1-
- U12 pad 5: /USB-C2/USB-C2.TX2+ -> /USB-C2/USB-C2.TX1+
- U12 pad 6: /USB-C2/USB-C2.TX2+ -> /USB-C2/USB-C2.TX1+
- U12 pad 7: /USB-C2/USB-C2.TX2- -> /USB-C2/USB-C2.TX1-
- U12 pad 9: /USB-C2/USB-C2.RX2+ -> /USB-C2/USB-C2.RX2-
- U28 pad 1: /USB-C_UP1/USB-C1.RX2- -> /USB-C_UP1/USB-C1.RX2+
- U28 pad 10: /USB-C_UP1/USB-C1.RX2- -> /USB-C_UP1/USB-C1.RX2+
- U28 pad 2: /USB-C_UP1/USB-C1.RX2+ -> /USB-C_UP1/USB-C1.RX2-
- U28 pad 4: /USB-C_UP1/USB-C1.TX2- -> /USB-C_UP1/USB-C1.TX1-
- U28 pad 5: /USB-C_UP1/USB-C1.TX2+ -> /USB-C_UP1/USB-C1.TX1+
- U28 pad 6: /USB-C_UP1/USB-C1.TX2+ -> /USB-C_UP1/USB-C1.TX1+
- U28 pad 7: /USB-C_UP1/USB-C1.TX2- -> /USB-C_UP1/USB-C1.TX1-
- U28 pad 9: /USB-C_UP1/USB-C1.RX2+ -> /USB-C_UP1/USB-C1.RX2-
- U29 pad 1: /USB-C_UP1/USB-C1.RX1- -> /USB-C_UP1/USB-C1.RX1+
- U29 pad 10: /USB-C_UP1/USB-C1.RX1- -> /USB-C_UP1/USB-C1.RX1+
- U29 pad 2: /USB-C_UP1/USB-C1.RX1+ -> /USB-C_UP1/USB-C1.RX1-
- U29 pad 4: /USB-C_UP1/USB-C1.TX1- -> /USB-C_UP1/USB-C1.TX2-
- U29 pad 5: /USB-C_UP1/USB-C1.TX1+ -> /USB-C_UP1/USB-C1.TX2+
- U29 pad 6: /USB-C_UP1/USB-C1.TX1+ -> /USB-C_UP1/USB-C1.TX2+
- U29 pad 7: /USB-C_UP1/USB-C1.TX1- -> /USB-C_UP1/USB-C1.TX2-
- U29 pad 9: /USB-C_UP1/USB-C1.RX1+ -> /USB-C_UP1/USB-C1.RX1-
- U6 pad 1: /USB-C1/USB-C1.RX2- -> /USB-C1/USB-C1.RX2+
- U6 pad 10: /USB-C1/USB-C1.RX2- -> /USB-C1/USB-C1.RX2+
- U6 pad 2: /USB-C1/USB-C1.RX2+ -> /USB-C1/USB-C1.RX2-
- U6 pad 4: /USB-C1/USB-C1.TX2- -> /USB-C1/USB-C1.TX1-
- U6 pad 5: /USB-C1/USB-C1.TX2+ -> /USB-C1/USB-C1.TX1+
- U6 pad 6: /USB-C1/USB-C1.TX2+ -> /USB-C1/USB-C1.TX1+
- U6 pad 7: /USB-C1/USB-C1.TX2- -> /USB-C1/USB-C1.TX1-
- U6 pad 9: /USB-C1/USB-C1.RX2+ -> /USB-C1/USB-C1.RX2-
- U7 pad 1: /USB-C1/USB-C1.RX1- -> /USB-C1/USB-C1.RX1+
- U7 pad 10: /USB-C1/USB-C1.RX1- -> /USB-C1/USB-C1.RX1+
- U7 pad 2: /USB-C1/USB-C1.RX1+ -> /USB-C1/USB-C1.RX1-
- U7 pad 4: /USB-C1/USB-C1.TX1- -> /USB-C1/USB-C1.TX2-
- U7 pad 5: /USB-C1/USB-C1.TX1+ -> /USB-C1/USB-C1.TX2+
- U7 pad 6: /USB-C1/USB-C1.TX1+ -> /USB-C1/USB-C1.TX2+
- U7 pad 7: /USB-C1/USB-C1.TX1- -> /USB-C1/USB-C1.TX2-
- U7 pad 9: /USB-C1/USB-C1.RX1+ -> /USB-C1/USB-C1.RX1-
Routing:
- net Net-(D13-C): track 0.00 -> 18.3 mm
- net Net-(U21-S-Pad1): track 0.00 -> 17.0 mm
- net /SD-interface/SD_D1: track 0.00 -> 15.0 mm
- net /SD-interface/SD_D2: track 0.00 -> 14.7 mm
- net /SD-interface/SD_D0: track 0.00 -> 14.5 mm
- net /SD-interface/SD_D3: track 0.00 -> 13.9 mm
- net /SD-interface/SD_CM: track 0.00 -> 13.0 mm
- net /SD-interface/SD_CK: track 0.00 -> 12.6 mm
- net Net-(U1-TEST1): track 8.92 -> 0.00 mm
- net Net-(U1-TEST2): track 7.05 -> 0.00 mm
- net +3V3_SD: track 0.00 -> 6.51 mm
- net /SD-interface/LED: track 0.00 -> 5.54 mm
- net Net-(U1-TEST3): track 5.30 -> 0.00 mm
- net GND: track 8.79 -> 13.3 mm
- net Net-(U21-G): track 4.09 -> 0.00 mm
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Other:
- board size 127.5 x 50.8 mm -> 119.5 x 91.8 mm
- board text added: "SD Card"
- board text added: "USB"
